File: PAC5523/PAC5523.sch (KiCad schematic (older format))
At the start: 67 parts, among them J2 U, J3 V, J4 W, Q1 Q_NMOS_GDS, T1 Transformer_1P_1S, U1 PAC5523

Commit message: updated schematic
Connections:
- net IUH: now also J2.3 (Pin_3); no longer J2.2 (Pin_2)
- net IVH: now also J3.3 (Pin_3); no longer J3.2 (Pin_2)
- net IWH: now also J4.3 (Pin_3); no longer J4.2 (Pin_2)
- net NTC_FET: now also J3.2 (Pin_2); no longer J3.3 (Pin_3)
- net U: now also J2.5 (Pin_5); no longer J2.4 (Pin_4)
- net V: now also J3.5 (Pin_5); no longer J3.4 (Pin_4)
- net W: now also J4.5 (Pin_5); no longer J4.4 (Pin_4)
- net at C3.1, D4.2 (A), R3.1: now also J2.4 (Pin_4); no longer J2.5 (Pin_5)
- net at C14.1, D9.2 (A), R11.1: now also J3.4 (Pin_4); no longer J3.5 (Pin_5)
- net at C16.1, D12.2 (A), R13.1: now also J4.4 (Pin_4); no longer J4.5 (Pin_5)
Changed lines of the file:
@@
 	1    0    0    -1
 $EndComp
-Wire Wire Line
-	10400 1500 9850 1500
 Connection ~ 9850 1500
 Wire Wire Line
@@
 	1    0    0    -1
 $EndComp
-Connection ~ 9850 3400
 Wire Wire Line
 	9850 3400 9350 3400
@@
 	9850 1250 10200 1250
 Wire Wire Line
-	10400 1400 10200 1400
-Wire Wire Line
-	10200 1400 10200 1850
-Wire Wire Line
 	9850 1850 10200 1850
-Text GLabel 10400 1700 0    50   Input ~ 0
+Text GLabel 10400 1600 0    50   Input ~ 0
 IUH
 Text GLabel 10400 1800 0    50   Input ~ 0
@@
 $EndComp
 Wire Wire Line
-	10200 3300 10200 3750
-Wire Wire Line
 	9850 3750 10200 3750
 Wire Wire Line
@@
 Text GLabel 10650 3700 0    50   Input ~ 0
 IVL
-Text GLabel 10650 3600 0    50   Input ~ 0
+Text GLabel 10650 3500 0    50   Input ~ 0
 IVH
 Connection ~ 9850 5300
-Wire Wire Line
-	10400 5300 9850 5300
 $Comp
 L Connector:Conn_01x06_Male J4
@@
 $EndComp
 Wire Wire Line
-	10400 5200 10200 5200
-Wire Wire Line
-	10200 5200 10200 5650
-Wire Wire Line
 	9850 5650 10200 5650
 Wire Wire Line
@@
 Text GLabel 10400 5600 0    50   Input ~ 0
 IWL
-Text GLabel 10400 5500 0    50   Input ~ 0
+Text GLabel 10400 5400 0    50   Input ~ 0
 IWH
 $Comp
@@
 Text GLabel 2400 2000 1    50   Input ~ 0
 NTC
-Text GLabel 10650 3500 0    50   Input ~ 0
+Text GLabel 10650 3600 0    50   Input ~ 0
 NTC_FET
-Wire Wire Line
-	9850 3400 10650 3400
-Wire Wire Line
-	10200 3300 10650 3300
 Wire Wire Line
 	10200 3200 10650 3200
@@
 Text Notes 5100 1550 0    50   ~ 0
 TVS Diode\nWiderstand
+Wire Wire Line
+	10650 3400 10200 3400
+Wire Wire Line
+	10200 3400 10200 3750
+Wire Wire Line
+	10650 3300 10100 3300
+Wire Wire Line
+	10100 3300 10100 3400
+Wire Wire Line
+	9850 3400 10100 3400
+Connection ~ 9850 3400
+Wire Wire Line
+	10100 5300 10100 5200
+Wire Wire Line
+	10100 5200 10400 5200
+Wire Wire Line
+	10100 5300 9850 5300
+Wire Wire Line
+	10400 5300 10200 5300
+Wire Wire Line
+	10200 5300 10200 5650
+Wire Wire Line
+	10100 1500 10100 1400
+Wire Wire Line
+	10100 1400 10400 1400
+Wire Wire Line
+	10100 1500 9850 1500
+Wire Wire Line
+	10400 1500 10200 1500
+Wire Wire Line
+	10200 1500 10200 1850
 $EndSCHEMATC

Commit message: wip
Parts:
- removed Q1: Q_NMOS_GDS, symbol Device:Q_NMOS_GDS
- removed T1: Transformer_1P_1S, symbol Device:Transformer_1P_1S
- added Q1: AON6276, Package_SON:VSONP-8-1EP_5x6_P1.27mm, symbol Device:Q_NMOS_SGD
- added U10: PA1137NL, otter:PA1137NL, symbol otter:PA1137NL
- J1: renamed from J4; footprint Connector_PinHeader_2.00mm:PinHeader_1x06_P2.00mm_Vertical -> otter:PinHeader_1x06_P2.00mm_Vertical_COMBI
- J2, J3: footprint Connector_PinHeader_2.00mm:PinHeader_1x06_P2.00mm_Vertical -> otter:PinHeader_1x06_P2.00mm_Vertical_COMBI
- R1: footprint Diode_SMD:D_0603_1608Metric -> Resistor_SMD:R_0805_2012Metric
- R10, R11, R12, R13, R15, R2, R3: footprint Diode_SMD:D_0805_2012Metric -> Resistor_SMD:R_0805_2012Metric
- R8, R9: footprint Diode_SMD:D_0603_1608Metric -> Resistor_SMD:R_0603_1608Metric
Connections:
- net NTC_FET is gone; now on net IVL: J3.2 (Pin_2)
- net NTC_FET_PAC is gone; now on net NTC: U1.45 (PF6/AD6)
- net CSM: now also Q1.1 (S)
- net ENC_A: no longer U1.38 (PE1)
- net ENC_B: no longer U1.39 (PE2)
- net ENC_ID: no longer U1.37 (PE0)
- net GNDPWR: now also U10.10, U10.9
- net HALL1: now also U1.37 (PE0); no longer U1.34 (PC4)
- net HALL2: now also U1.38 (PE1); no longer U1.35 (PC5)
- net IUL: now also J2.2 (Pin_2); no longer J2.1 (Pin_1)
- net IVL: no longer J3.1 (Pin_1)
- net IWL: now also J1.2 (Pin_2); no longer J1.1 (Pin_1)
- net NTC: no longer U1.46 (PF5/AD5)
- net U: now also J2.6 (Pin_6); no longer J2.5 (Pin_5)
- net V: now also J3.6 (Pin_6); no longer J3.5 (Pin_5)
- net VSYS: no longer C10.1, C28.1, C34.1
- net W: now also J1.6 (Pin_6); no longer J1.5 (Pin_5)
- net at C2.2, D3.2 (A), R2.1: now also J2.5 (Pin_5); no longer J2.6 (Pin_6)
- net at C13.2, D8.2 (A), R10.1: now also J3.5 (Pin_5); no longer J3.6 (Pin_6)
- net at C15.2, D11.2 (A), R12.1: now also J1.5 (Pin_5); no longer J1.6 (Pin_6)
- net at C20.1, C21.1, C32.1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: now also U10.4
- net at D16.2 (A): now also Q1.3 (D), U10.3
- net at D14.2 (A): now also U10.7, U10.8
- net at R15.2: now also Q1.2 (G)
- net UART_RX: no longer names the net of U1.48 (PF3)
- net UART_TX: no longer names the net of U1.1 (PF2)
- new net +5V: C10.1, C28.1, C34.1
- new net CANRX: U1.34 (PC4)
- new net CANTX: U1.35 (PC5)
- new net CLK: U1.39 (PE2)
- new net NTC_EXT: U1.46 (PF5/AD5)
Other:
- moved on the sheet: C25, C33, D14

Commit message: wip
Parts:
- D1, D10, D11, D12, D13, D14, D15, D16, D2, D3, D4, D5, D6, D7, D8, D9: footprint Diode_SMD:D_SMA -> Diode_SMD:D_SOD-123F
- R14: footprint Resistor_SMD:R_2512_6332Metric -> Resistor_SMD:R_0805_2012Metric
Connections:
- net +5V: now also C26.1
- net 3V3: no longer C26.1
- net HALL1: now also U1.36 (PC6); no longer U1.37 (PE0)
- net HALL2: now also U1.37 (PE0); no longer U1.38 (PE1)
- net HALL3: now also U1.38 (PE1); no longer U1.36 (PC6)
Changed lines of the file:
@@
 F 0 "D1" V 8854 1718 50  0000 L CNN
 F 1 "SS310" V 8945 1718 50  0000 L CNN
-F 2 "Diode_SMD:D_SMA" V 8900 1650 50  0001 C CNN
+F 2 "Diode_SMD:D_SOD-123F" V 8900 1650 50  0001 C CNN
 F 3 "~" V 8900 1650 50  0001 C CNN
 	1    8900 1650
@@
 F 0 "D2" H 9550 1105 50  0000 C CNN
 F 1 "SS310" H 9550 1014 50  0000 C CNN
-F 2 "Diode_SMD:D_SMA" V 9550 900 50  0001 C CNN
+F 2 "Diode_SMD:D_SOD-123F" V 9550 900 50  0001 C CNN
 F 3 "~" V 9550 900 50  0001 C CNN
 	1    9550 900
@@
 F 0 "D3" H 9550 1355 50  0000 C CNN
 F 1 "SS310" H 9550 1264 50  0000 C CNN
-F 2 "Diode_SMD:D_SMA" V 9550 1150 50  0001 C CNN
+F 2 "Diode_SMD:D_SOD-123F" V 9550 1150 50  0001 C CNN
 F 3 "~" V 9550 1150 50  0001 C CNN
 	1    9550 1150
@@
 F 0 "D4" H 9550 2000 50  0000 C CNN
 F 1 "SS310" H 9550 1900 50  0000 C CNN
-F 2 "Diode_SMD:D_SMA" V 9550 1750 50  0001 C CNN
+F 2 "Diode_SMD:D_SOD-123F" V 9550 1750 50  0001 C CNN
 F 3 "~" V 9550 1750 50  0001 C CNN
 	1    9550 1750
@@
 F 0 "D5" V 8854 3618 50  0000 L CNN
 F 1 "SS310" V 8945 3618 50  0000 L CNN
-F 2 "Diode_SMD:D_SMA" V 8900 3550 50  0001 C CNN
+F 2 "Diode_SMD:D_SOD-123F" V 8900 3550 50  0001 C CNN
 F 3 "~" V 8900 3550 50  0001 C CNN
 	1    8900 3550
@@
 F 0 "D7" H 9550 3005 50  0000 C CNN
 F 1 "SS310" H 9550 2914 50  0000 C CNN
-F 2 "Diode_SMD:D_SMA" V 9550 2800 50  0001 C CNN
+F 2 "Diode_SMD:D_SOD-123F" V 9550 2800 50  0001 C CNN
 F 3 "~" V 9550 2800 50  0001 C CNN
 	1    9550 2800
@@
 F 0 "D8" H 9550 3255 50  0000 C CNN
 F 1 "SS310" H 9550 3164 50  0000 C CNN
-F 2 "Diode_SMD:D_SMA" V 9550 3050 50  0001 C CNN
+F 2 "Diode_SMD:D_SOD-123F" V 9550 3050 50  0001 C CNN
 F 3 "~" V 9550 3050 50  0001 C CNN
 	1    9550 3050
@@
 F 0 "D9" H 9550 3900 50  0000 C CNN
 F 1 "SS310" H 9550 3800 50  0000 C CNN
-F 2 "Diode_SMD:D_SMA" V 9550 3650 50  0001 C CNN
+F 2 "Diode_SMD:D_SOD-123F" V 9550 3650 50  0001 C CNN
 F 3 "~" V 9550 3650 50  0001 C CNN
 	1    9550 3650
@@
 F 0 "D6" V 8854 5518 50  0000 L CNN
 F 1 "SS310" V 8945 5518 50  0000 L CNN
-F 2 "Diode_SMD:D_SMA" V 8900 5450 50  0001 C CNN
+F 2 "Diode_SMD:D_SOD-123F" V 8900 5450 50  0001 C CNN
 F 3 "~" V 8900 5450 50  0001 C CNN
 	1    8900 5450
@@
 F 0 "D10" H 9550 4905 50  0000 C CNN
 F 1 "SS310" H 9550 4814 50  0000 C CNN
-F 2 "Diode_SMD:D_SMA" V 9550 4700 50  0001 C CNN
+F 2 "Diode_SMD:D_SOD-123F" V 9550 4700 50  0001 C CNN
 F 3 "~" V 9550 4700 50  0001 C CNN
 	1    9550 4700
@@
 F 0 "D11" H 9550 5155 50  0000 C CNN
 F 1 "SS310" H 9550 5064 50  0000 C CNN
-F 2 "Diode_SMD:D_SMA" V 9550 4950 50  0001 C CNN
+F 2 "Diode_SMD:D_SOD-123F" V 9550 4950 50  0001 C CNN
 F 3 "~" V 9550 4950 50  0001 C CNN
 	1    9550 4950
@@
 F 0 "D12" H 9550 5800 50  0000 C CNN
 F 1 "SS310" H 9550 5700 50  0000 C CNN
-F 2 "Diode_SMD:D_SMA" V 9550 5550 50  0001 C CNN
+F 2 "Diode_SMD:D_SOD-123F" V 9550 5550 50  0001 C CNN
 F 3 "~" V 9550 5550 50  0001 C CNN
 	1    9550 5550
@@
 Wire Wire Line
 	10350 1950 10350 2000
+Text GLabel 2850 4650 3    50   Input ~ 0
+HALL1
 Text GLabel 2250 4650 3    50   Input ~ 0
-HALL1
+HALL2
 Text GLabel 2350 4650 3    50   Input ~ 0
-HALL2
-Text GLabel 2850 4650 3    50   Input ~ 0
 HALL3
 Text GLabel 3550 4050 2    50   Input ~ 0
@@
 F 0 "D15" H 5700 895 50  0000 C CNN
 F 1 "SS310" H 5700 986 50  0000 C CNN
-F 2 "Diode_SMD:D_SMA" V 5700 1100 50  0001 C CNN
+F 2 "Diode_SMD:D_SOD-123F" V 5700 1100 50  0001 C CNN
 F 3 "~" V 5700 1100 50  0001 C CNN
 	1    5700 1100
@@
 F 0 "D13" H 4750 1445 50  0000 C CNN
 F 1 "SS310" H 4750 1536 50  0000 C CNN
-F 2 "Diode_SMD:D_SMA" V 4750 1650 50  0001 C CNN
+F 2 "Diode_SMD:D_SOD-123F" V 4750 1650 50  0001 C CNN
 F 3 "~" V 4750 1650 50  0001 C CNN
 	1    4750 1650
@@
 F 0 "D14" H 6800 1445 50  0000 C CNN
 F 1 "SS310" H 6800 1536 50  0000 C CNN
-F 2 "Diode_SMD:D_SMA" V 6800 1650 50  0001 C CNN
+F 2 "Diode_SMD:D_SOD-123F" V 6800 1650 50  0001 C CNN
 F 3 "~" V 6800 1650 50  0001 C CNN
 	1    6800 1650
@@
 F 0 "R14" H 6059 2746 50  0000 L CNN
 F 1 "TBD" H 6059 2655 50  0000 L CNN
-F 2 "Resistor_SMD:R_2512_6332Metric" H 6000 2700 50  0001 C CNN
+F 2 "Resistor_SMD:R_0805_2012Metric" H 6000 2700 50  0001 C CNN
 F 3 "~" H 6000 2700 50  0001 C CNN
 	1    6000 2700
@@
 F 0 "D16" V 5754 2018 50  0000 L CNN
 F 1 "SS310" V 5845 2018 50  0000 L CNN
-F 2 "Diode_SMD:D_SMA" V 5800 1950 50  0001 C CNN
+F 2 "Diode_SMD:D_SOD-123F" V 5800 1950 50  0001 C CNN
 F 3 "~" V 5800 1950 50  0001 C CNN
 	1    5800 1950
@@
 Text GLabel 2900 2000 1    50   Input ~ 0
 SWDCL
-Text GLabel 2100 5700 1    50   Input ~ 0
-UART_TX
-Text GLabel 2200 5700 1    50   Input ~ 0
-UART_RX
 Text GLabel 10100 3400 3    50   Input ~ 0
 V
@@
 	1    0    0    -1
 $EndComp
-Text GLabel 6650 4850 1    50   Input ~ 0
-3V3
 Text GLabel 5600 4850 1    50   Input ~ 0
 3V3
@@
 Text GLabel 2750 4650 3    50   Input ~ 0
 CANTX
-Text GLabel 2100 5700 3    50   Input ~ 0
-CANRX
-Text GLabel 2200 5700 3    50   Input ~ 0
-CANTX
+$Comp
+L power:+5V #PWR?
+U 1 1 5CD10758
+P 6650 4850
+AR Path="/5D5C3A79/5CD10758" Ref="#PWR?"  Part="1"
+AR Path="/5CD10758" Ref="#PWR0148"  Part="1"
+F 0 "#PWR0148" H 6650 4700 50  0001 C CNN
+F 1 "+5V" V 6665 4978 50  0000 L CNN
+F 2 "" H 6650 4850 50  0001 C CNN
+F 3 "" H 6650 4850 50  0001 C CNN
+	1    6650 4850
+	1    0    0    -1
+$EndComp
 $EndSCHEMATC

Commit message: wip
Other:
- note added: "Todo:\nOszillator\nNTC mergen\nEncoder\n"
- note removed: "Todo:\nBuchsen\nFootprints!\n"
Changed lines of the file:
@@
 IUH
 Text Notes 3700 1200 0    50   ~ 0
-Todo:\nBuchsen\nFootprints!\n
+Todo:\nOszillator\nNTC mergen\nEncoder\n
 $Comp
 L Connector:Conn_01x06_Male J2

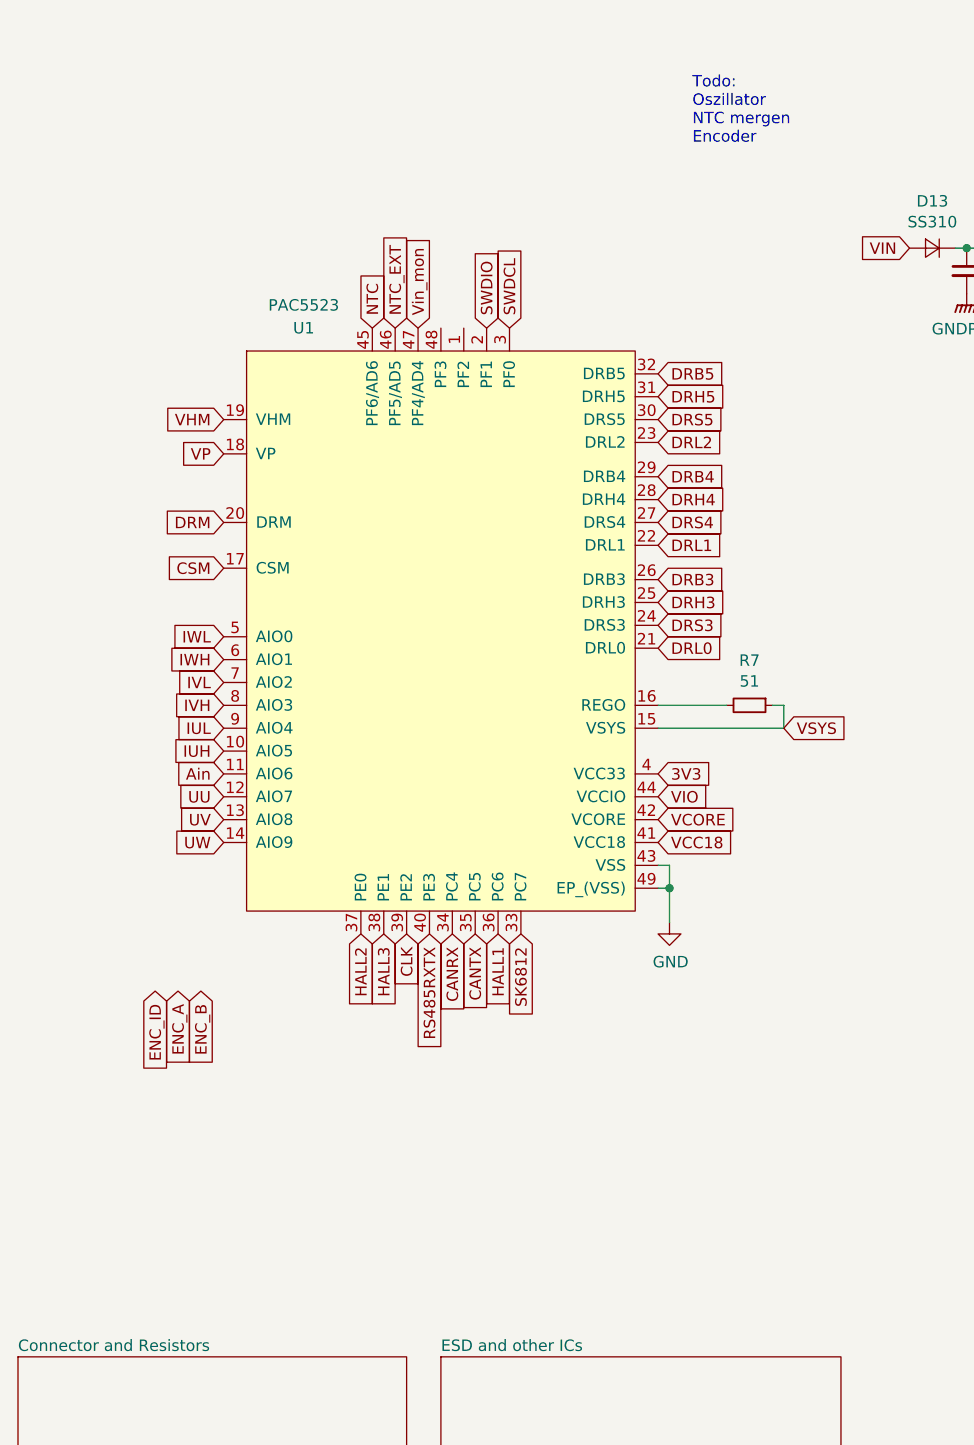
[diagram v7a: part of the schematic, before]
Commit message: added Encoder,LED,NTC
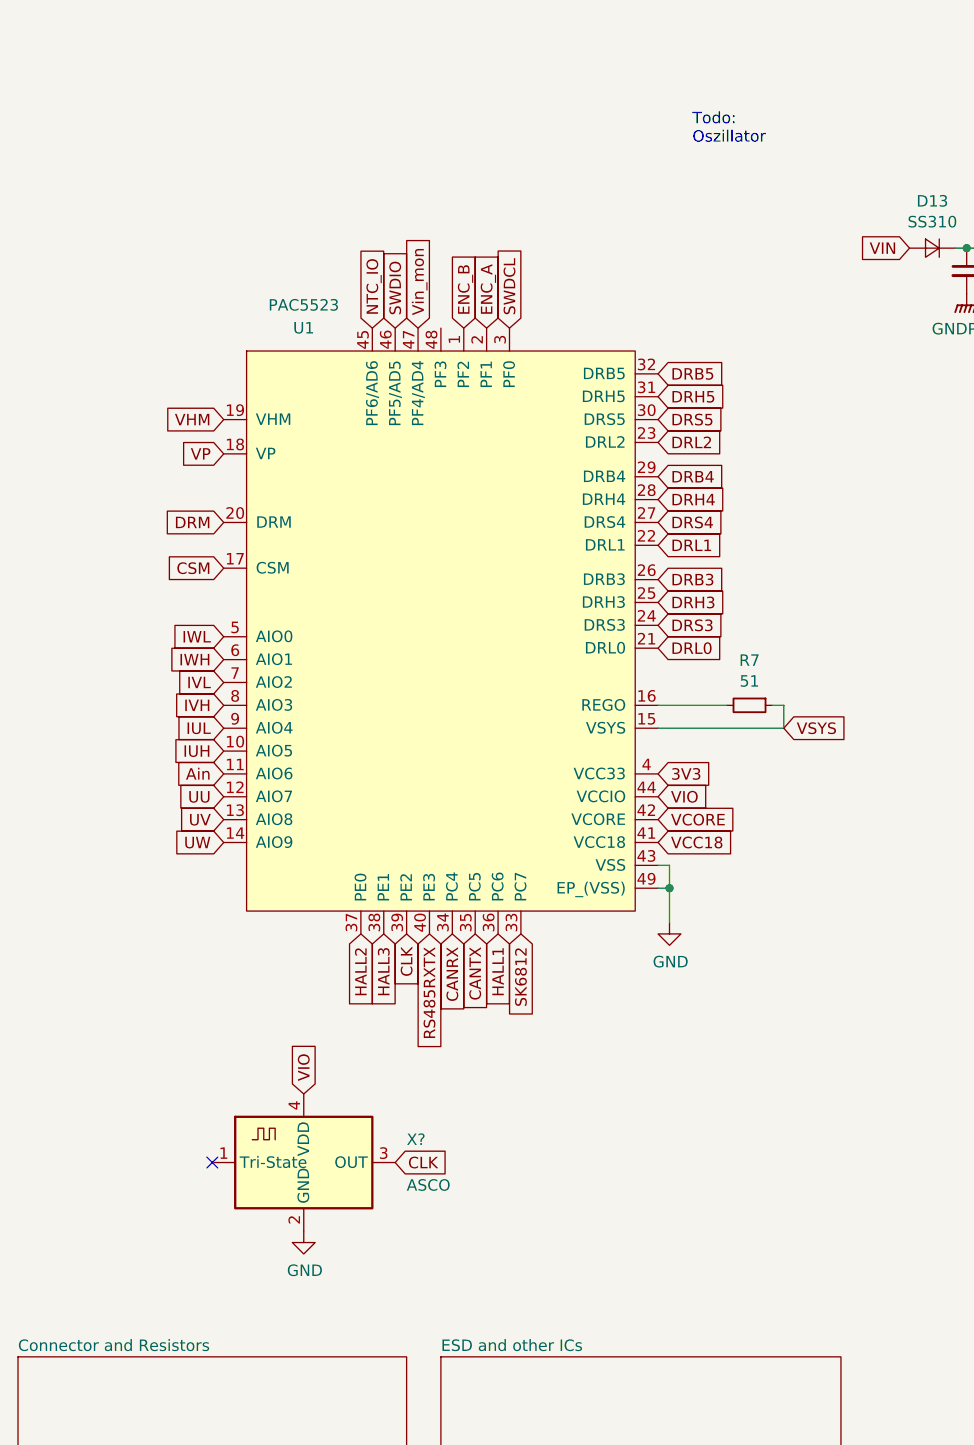
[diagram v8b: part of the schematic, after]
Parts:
- added X?: ASCO, Oscillator:Oscillator_SMD_Abracon_ASCO-4Pin_1.6x1.2mm, symbol Oscillator:ASCO
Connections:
- net NTC_EXT is gone; now on net SWDIO: U1.46 (PF5/AD5)
- net CLK: now also X?.3 (OUT)
- net ENC_A: now also U1.2 (PF1)
- net ENC_B: now also U1.1 (PF2)
- net GND: now also X?.2 (GND)
- net SWDIO: no longer U1.2 (PF1)
- net VIO: now also X?.4 (VDD)
- net NTC renamed NTC_IO
- no-connect marks 0 -> 1
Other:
- note added: "Todo:\nOszillator\n"
- note removed: "Todo:\nOszillator\nNTC mergen\nEncoder\n"
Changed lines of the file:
@@
 IUH
 Text Notes 3700 1200 0    50   ~ 0
-Todo:\nOszillator\nNTC mergen\nEncoder\n
+Todo:\nOszillator\n
 $Comp
 L Connector:Conn_01x06_Male J2
@@
 Wire Wire Line
 	6000 2050 5800 2050
-Text GLabel 2800 2000 1    50   Input ~ 0
+Text GLabel 2400 2000 1    50   Input ~ 0
 SWDIO
 Text GLabel 2900 2000 1    50   Input ~ 0
@@
 Text GLabel 2500 2000 1    50   Input ~ 0
 Vin_mon
-Text GLabel 2400 2000 1    50   Input ~ 0
-NTC_EXT
 Text GLabel 3550 4150 2    50   Input ~ 0
 VCORE
 Text GLabel 3550 4250 2    50   Input ~ 0
 VCC18
-Text GLabel 2300 2000 1    50   Input ~ 0
-NTC
 Text GLabel 6000 2550 2    50   Input ~ 0
 CSM
@@
 Text GLabel 2550 4650 3    50   Input ~ 0
 RS485RXTX
-Text GLabel 1350 4900 3    50   Input ~ 0
-ENC_ID
-Text GLabel 1450 4900 3    50   Input ~ 0
+Text GLabel 2800 2000 1    50   Input ~ 0
 ENC_A
-Text GLabel 1550 4900 3    50   Input ~ 0
+Text GLabel 2700 2000 1    50   Input ~ 0
 ENC_B
 Text GLabel 2950 4650 3    50   Input ~ 0
@@
 	1    0    0    -1
 $EndComp
+Text GLabel 2300 2000 1    50   Input ~ 0
+NTC_IO
+$Comp
+L Oscillator:ASCO X?
+U 1 1 5CE0A013
+P 2000 5650
+F 0 "X?" H 2450 5750 50  0000 L CNN
+F 1 "ASCO" H 2450 5550 50  0000 L CNN
+F 2 "Oscillator:Oscillator_SMD_Abracon_ASCO-4Pin_1.6x1.2mm" H 2100 5300 50  0001 C CNN
+F 3 "https://abracon.com/Oscillators/ASCO.pdf" H 1775 5775 50  0001 C CNN
+	1    2000 5650
+	1    0    0    -1
+$EndComp
+Text GLabel 2400 5650 2    50   Input ~ 0
+CLK
+Text GLabel 2000 5350 1    50   Input ~ 0
+VIO
+$Comp
+L power:GND #PWR?
+U 1 1 5CE19C05
+P 2000 5950
+F 0 "#PWR?" H 2000 5700 50  0001 C CNN
+F 1 "GND" H 2005 5777 50  0000 C CNN
+F 2 "" H 2000 5950 50  0001 C CNN
+F 3 "" H 2000 5950 50  0001 C CNN
+	1    2000 5950
+	1    0    0    -1
+$EndComp
+NoConn ~ 1600 5650
 $EndSCHEMATC
